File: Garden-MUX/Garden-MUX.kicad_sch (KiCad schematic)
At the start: 56 parts, among them J1 USB_C_Receptacle_USB2.0_16P, J2 SDCARD_MODULE, P1 S2B-PH-SM4-TB, Q1 AO3401A, U1 ESP32-C6-MINI-1, U2 MCP73832-2-OT, U3 AP2112K-3.3, U4 AP2112K-3.3

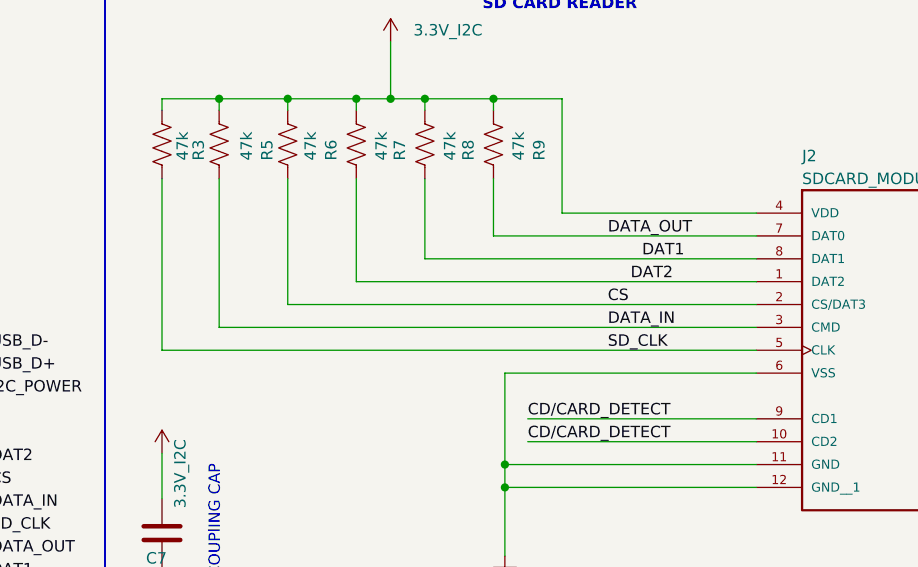
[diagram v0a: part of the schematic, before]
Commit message: Adjust position of 3d models
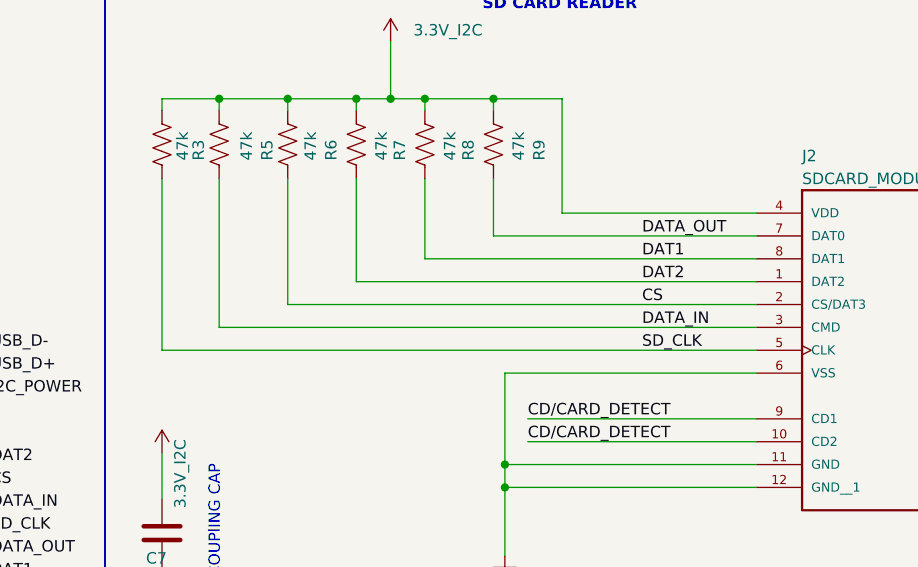
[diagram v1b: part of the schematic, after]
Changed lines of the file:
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@@
-	(wire
-		(pts
-			(xy 445.77 55.88) (xy 379.73 55.88)
-		)
-		(stroke
-			(width 0)
-			(type default)
-		)
-	)
 	(wire
 		(pts
@@
 	(wire
 		(pts
+			(xy 393.7 50.8) (xy 445.77 50.8)
+		)
+		(stroke
+			(width 0)
+			(type default)
+		)
+	)
+	(wire
+		(pts
 			(xy 417.83 68.58) (xy 417.83 71.12)
 		)
@@
 	(wire
 		(pts
+			(xy 401.32 48.26) (xy 445.77 48.26)
+		)
+		(stroke
+			(width 0)
+			(type default)
+		)
+	)
+	(wire
+		(pts
 			(xy 401.32 48.26) (xy 401.32 36.83)
 		)
@@
 	(wire
 		(pts
-			(xy 445.77 50.8) (xy 393.7 50.8)
-		)
-		(stroke
-			(width 0)
-			(type default)
-		)
-	)
-	(wire
-		(pts
 			(xy 467.36 144.78) (xy 464.82 144.78)
 		)
@@
 	(wire
 		(pts
-			(xy 445.77 48.26) (xy 401.32 48.26)
-		)
-		(stroke
-			(width 0)
-			(type default)
-		)
-	)
-	(wire
-		(pts
 			(xy 26.67 106.68) (xy 26.67 111.76)
 		)
@@
 		(pts
 			(xy 557.53 76.2) (xy 570.23 76.2)
+		)
+		(stroke
+			(width 0)
+			(type default)
+		)
+	)
+	(wire
+		(pts
+			(xy 379.73 55.88) (xy 445.77 55.88)
 		)
 		(stroke
@@
 	)
 	(label "DATA_IN"
-		(at 429.26 53.34 0)
+		(at 433.07 53.34 0)
 		(effects
 			(font
@@
 	)
 	(label "CS"
-		(at 429.26 50.8 0)
+		(at 433.07 50.8 0)
 		(effects
 			(font
@@
 	)
 	(label "SD_CLK"
-		(at 429.26 55.88 0)
+		(at 433.07 55.88 0)
 		(effects
 			(font
@@
 	)
 	(label "DATA_OUT"
-		(at 429.26 43.18 0)
+		(at 433.07 43.18 0)
 		(effects
 			(font
@@
 	)
 	(label "DAT2"
-		(at 431.8 48.26 0)
-		(effects
-			(font
+		(at 433.07 48.26 0)
+		(effects
+			(font

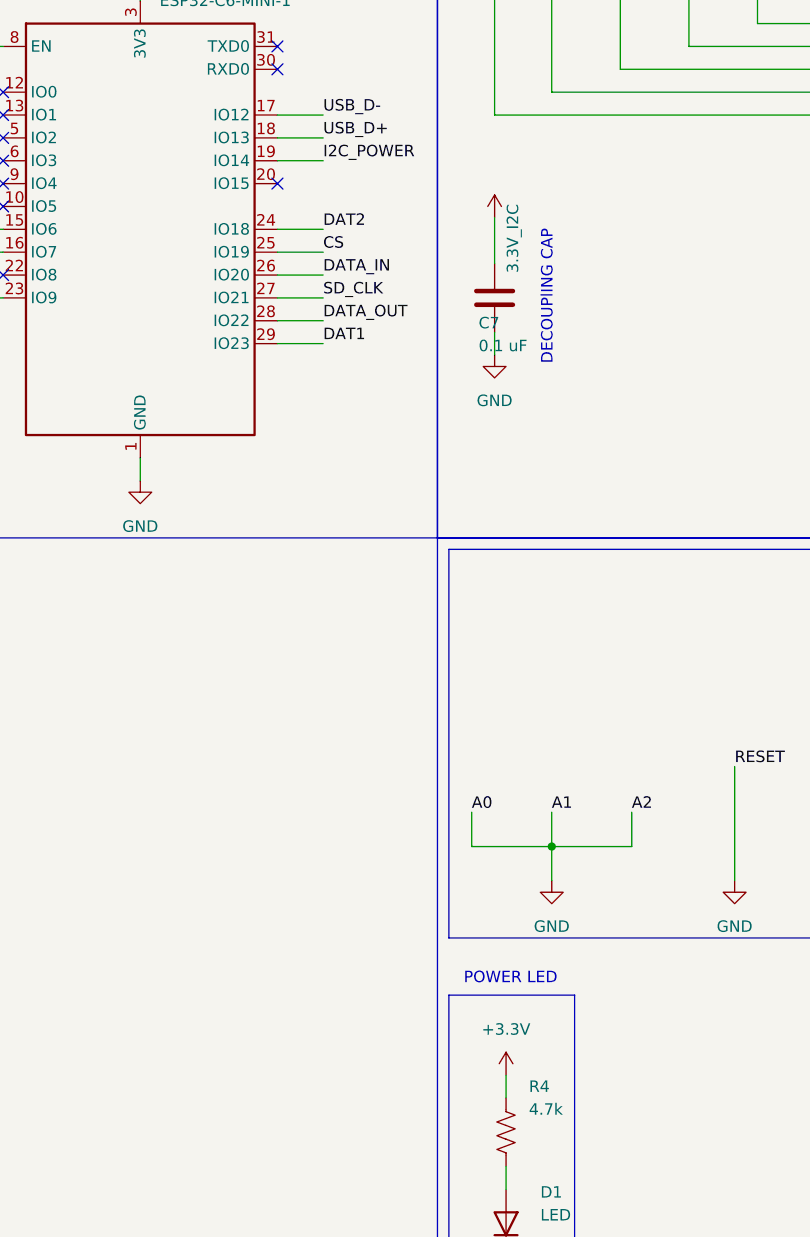
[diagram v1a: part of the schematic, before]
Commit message: Switch red LED to IO15
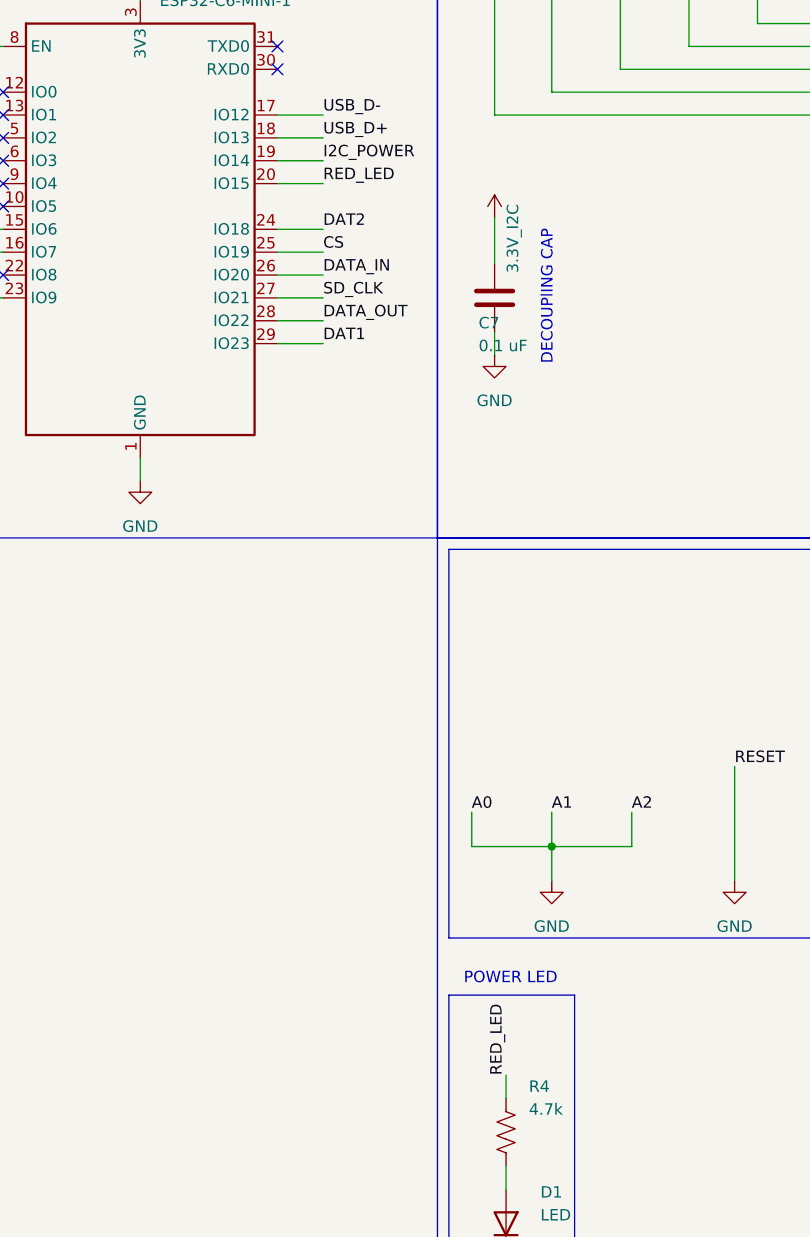
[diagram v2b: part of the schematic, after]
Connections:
- net +3.3V: no longer R4.1
- net RED_LED: now reaches U1.20 (IO15)
- net RED_LED: now also R4.1
- no-connect marks 13 -> 12
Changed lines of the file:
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@@
 	)
 	(no_connect
-		(at 355.6 63.5)
-	)
-	(no_connect
 		(at 325.12 63.5)
 	)
@@
 	(wire
 		(pts
+			(xy 355.6 63.5) (xy 360.68 63.5)
+		)
+		(stroke
+			(width 0)
+			(type default)
+		)
+	)
+	(wire
+		(pts
 			(xy 551.18 130.81) (xy 548.64 130.81)
 		)
@@
 		)
 	)
+	(label "RED_LED"
+		(at 381 162.56 90)
+		(effects
+			(font
+				(size 1.27 1.27)
+			)
+			(justify left bottom)
+		)
+	)
 	(label "SCL6"
 		(at 110.49 105.41 0)
@@
 		)
 	)
+	(label "RED_LED"
+		(at 360.68 63.5 0)
+		(effects
+			(font
+				(size 1.27 1.27)
+			)
+			(justify left bottom)
+		)
+	)
 	(label "SCL3"
 		(at 50.8 137.16 0)
@@
 					(unit 1)
 				)
-			)
-		)
-	)
-	(symbol
-		(lib_id "power:+3V3")
-		(at 381 162.56 0)
-		(unit 1)
-		(exclude_from_sim no)
-		(in_bom yes)
-		(on_board yes)
-		(dnp no)
-		(property "Reference" "#PWR044"
-			(at 381 166.37 0)
-			(effects
-				(font
-					(size 1.27 1.27)
-				)
-				(hide yes)
-			)
-		)
-		(property "Value" "+3.3V"
-			(at 381 157.48 0)
-			(effects
-				(font
-					(size 1.27 1.27)
-				)
-			)
-		)
-		(property "Footprint" ""
-			(at 381 162.56 0)
-			(effects
-				(font
-					(size 1.27 1.27)
-				)
-				(hide yes)
-			)
-		)
-		(property "Datasheet" ""
-			(at 381 162.56 0)
-			(effects
-				(font
-					(size 1.27 1.27)
-				)
-				(hide yes)
-			)
-		)
-		(property "Description" "Power symbol creates a global label with name \"+3V3\""
-			(at 381 162.56 0)
-			(effects
-				(font
-					(size 1.27 1.27)
-				)
-				(hide yes)
-			)
-		)
-		(pin "1"
-		)
-		(instances
-			(project "Garden-MUX"
-				(path "/27ca7141-07bc-42d4-b74a-f55a9e480797"
-					(reference "#PWR044")
-					(unit 1)
-				)

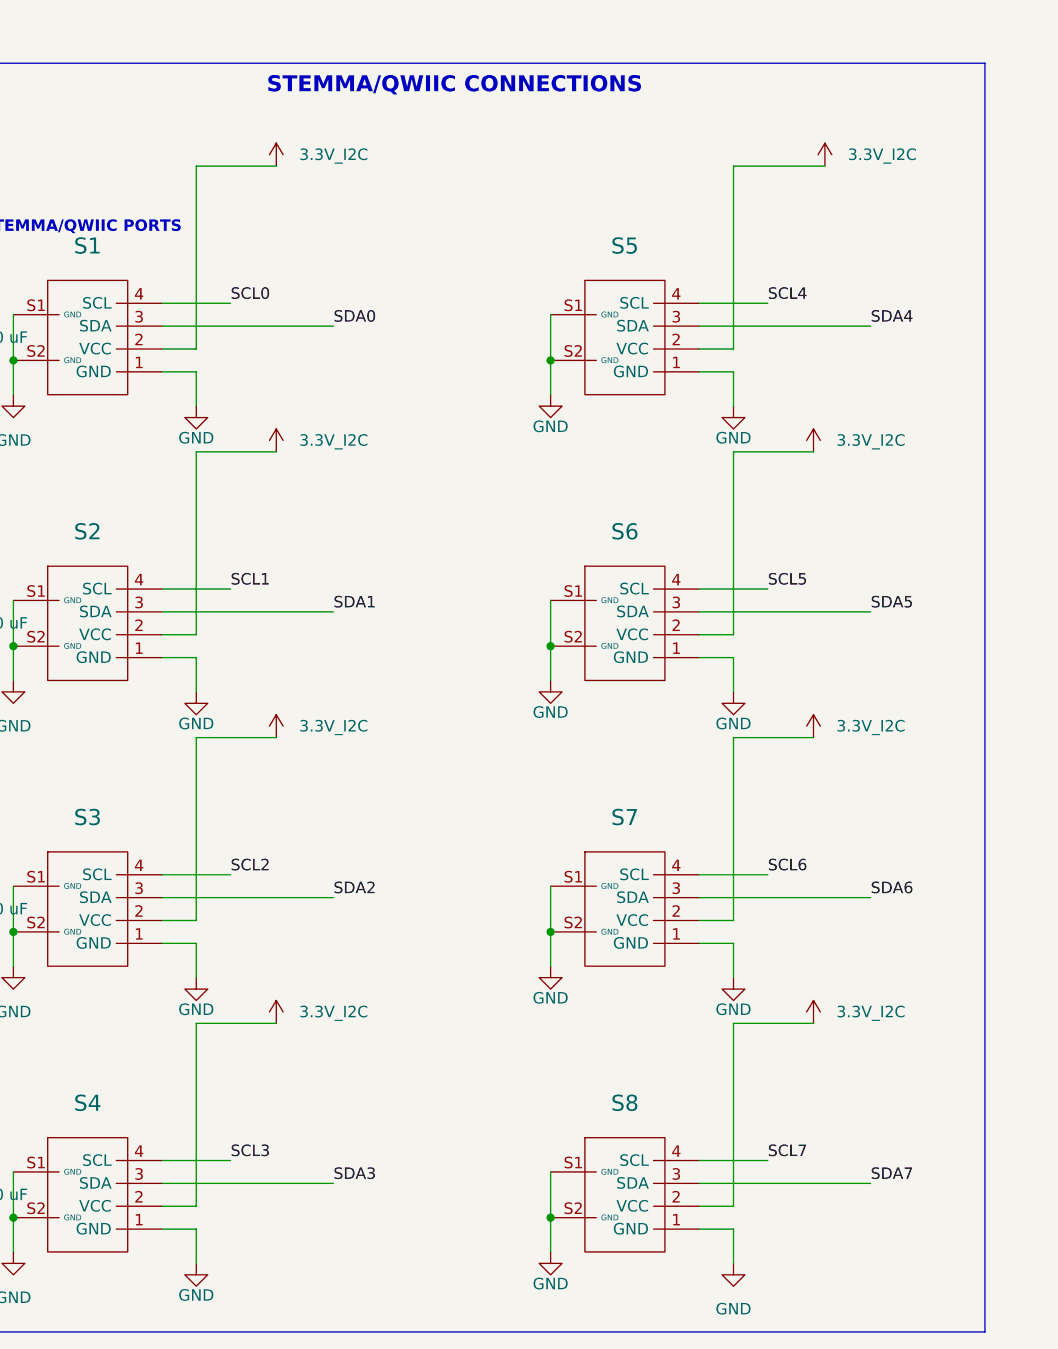
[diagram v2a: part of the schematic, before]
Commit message: Move decaps and resistors to the left
Start the process of moving 3.3v components further to the right to allow room for pull-up resistors.
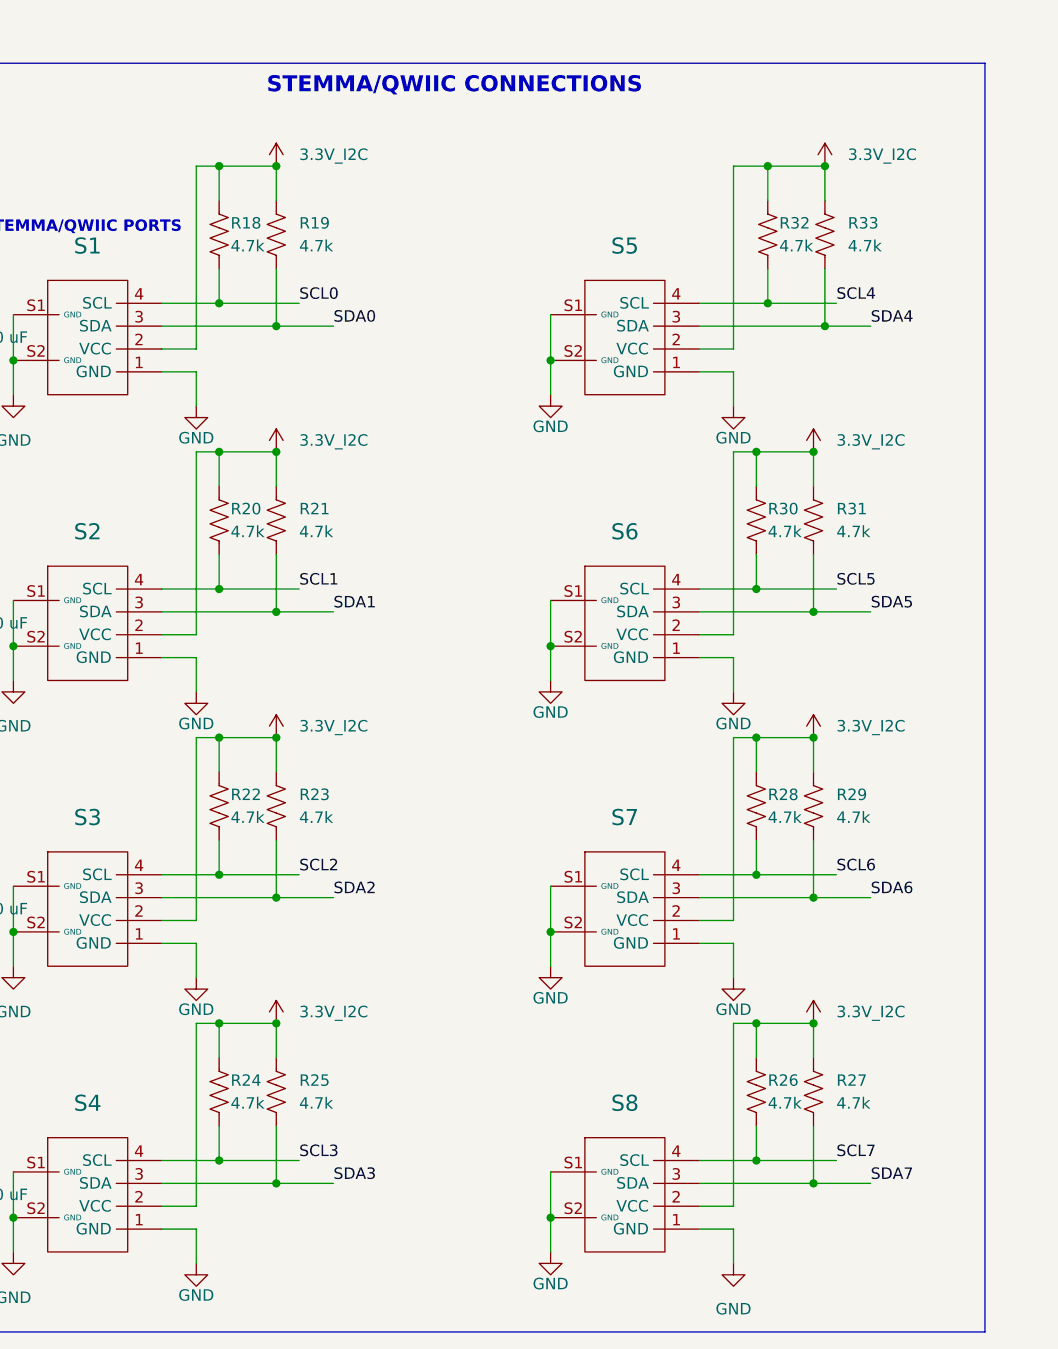
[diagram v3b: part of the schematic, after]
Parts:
- added R18, R19, R20, R21, R22, R23, R24, R25, R26, R27, R28, R29, R30, R31, R32, R33: 4.7k, Resistor_SMD:R_0603_1608Metric, symbol Device:R_US
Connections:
- net 3.3V_I2C: now also R18.1, R19.1, R20.1, R21.1, R22.1, R23.1, R24.1, R25.1, R26.1, R27.1, R28.1, R29.1, R30.1, R31.1, R32.1, R33.1
- net SCL0: now also R18.2
- net SCL1: now also R20.2
- net SCL2: now also R22.2
- net SCL3: now also R24.2
- net SCL4: now also R32.2
- net SCL5: now also R30.2
- net SCL6: now also R28.2
- net SCL7: now also R26.2
- net SDA0: now also R19.2
- net SDA1: now also R21.2
- net SDA2: now also R23.2
- net SDA3: now also R25.2
- net SDA4: now also R33.2
- net SDA5: now also R31.2
- net SDA6: now also R29.2
- net SDA7: now also R27.2
